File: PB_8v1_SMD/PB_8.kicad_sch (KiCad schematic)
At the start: 26 parts, among them J18 Power In Right, J23 VIN Voltage, J25 RTC Conn, J26 OLED Conn, J27 GPIO Header, J28 Aux Pwr, J29 VIN Select, Q1 DMP3056L, SW1 Enter BTN, SW2 Down BTN, SW3 OLED Select, U1 OKI-78SR-5, U2 24LC256

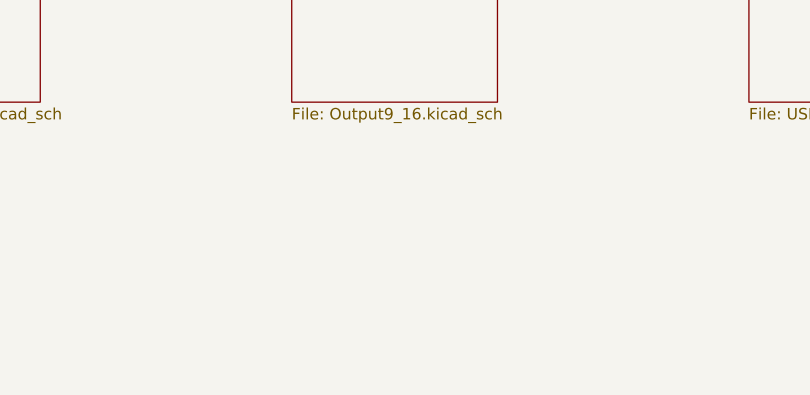
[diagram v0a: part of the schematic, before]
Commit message: Add Diff out 9-12
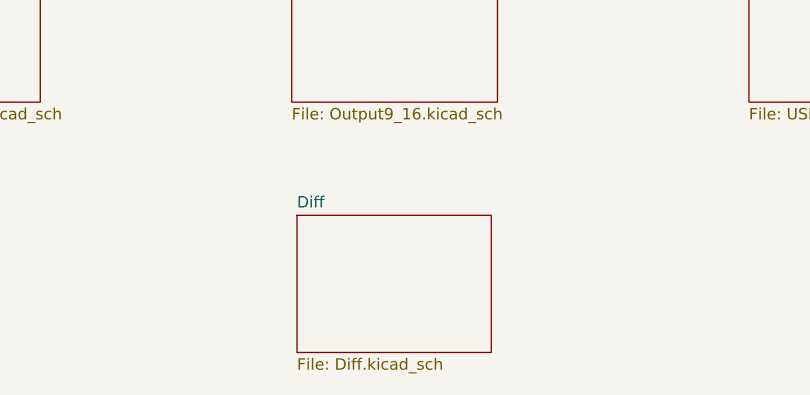
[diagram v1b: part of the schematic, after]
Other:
- added sheet Diff (Diff.kicad_sch)
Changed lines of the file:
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@@
+    )
+  )
+  (sheet (at 87.3252 177.292) (size 21.59 15.24) (fields_autoplaced)
+    (stroke (width 0) (type solid) (color 0 0 0 0))
+    (fill (color 0 0 0 0.0000))
+    (property "Sheet name" "Diff" (id 0) (at 87.3252 176.5804 0)
+      (effects (font (size 1.27 1.27)) (justify left bottom))
+    )
+    (property "Sheet file" "Diff.kicad_sch" (id 1) (at 87.3252 193.1166 0)
+      (effects (font (size 1.27 1.27)) (justify left top))
     )
   )
@@
     (path "/" (page "1"))
     (path "/00000000-0000-0000-0000-00005d413c25" (page "2"))
+    (path "/ee281e36-0822-48a2-9e3f-ba9140af478c" (page "3"))
     (path "/00000000-0000-0000-0000-00005d4698de" (page "4"))
     (path "/00000000-0000-0000-0000-00005d648680" (page "6"))
   )
   (symbol_instances
+    (path "/ee281e36-0822-48a2-9e3f-ba9140af478c/97fca2e9-9c9d-485a-af6f-c9d488a151a9"
+      (reference "#PWR01") (unit 1) (value "+5V") (footprint "")
+    )
     (path "/00000000-0000-0000-0000-00005d5b866e"
       (reference "#PWR02") (unit 1) (value "GND") (footprint "")
     )
+    (path "/ee281e36-0822-48a2-9e3f-ba9140af478c/39d41e00-f438-4796-a9cd-e6f3168c73de"
+      (reference "#PWR03") (unit 1) (value "GND") (footprint "")
+    )
     (path "/00000000-0000-0000-0000-00005d51c5e3"
       (reference "#PWR04") (unit 1) (value "GND") (footprint "")
@@
       (reference "#PWR032") (unit 1) (value "+3.3V") (footprint "")
     )
+    (path "/ee281e36-0822-48a2-9e3f-ba9140af478c/78855180-3489-4b90-8473-a0526a6cdc7e"
+      (reference "#PWR033") (unit 1) (value "+5V") (footprint "")
+    )
+    (path "/ee281e36-0822-48a2-9e3f-ba9140af478c/8ec2d9bf-7f3e-41fd-b41a-95a7b12782d3"
+      (reference "#PWR034") (unit 1) (value "GND") (footprint "")
+    )
     (path "/00000000-0000-0000-0000-00005d413c25/00000000-0000-0000-0000-00005e95876a"
       (reference "#PWR038") (unit 1) (value "GND") (footprint "")
@@
       (reference "C4") (unit 1) (value "0.1uF") (footprint "Capacitor_SMD:C_0603_1608Metric_Pad1.08x0.95mm_HandSolder")
     )
+    (path "/ee281e36-0822-48a2-9e3f-ba9140af478c/9afffebf-f2b4-422d-b595-02654a91f956"
+      (reference "C5") (unit 1) (value "0.1uF") (footprint "Capacitor_SMD:C_0603_1608Metric_Pad1.08x0.95mm_HandSolder")
+    )
     (path "/00000000-0000-0000-0000-00005d4698de/00000000-0000-0000-0000-00005d4e3ada"
       (reference "C6") (unit 1) (value "0.1uF") (footprint "Capacitor_SMD:C_0603_1608Metric_Pad1.08x0.95mm_HandSolder")
@@
       (reference "J8") (unit 1) (value "String8") (footprint "Connector_Phoenix_MC:PhoenixContact_MCV_1,5_3-G-3.5_1x03_P3.50mm_Vertical")
     )
+    (path "/ee281e36-0822-48a2-9e3f-ba9140af478c/383a15f1-ee32-4530-bca5-9032d1bb1254"
+      (reference "J9") (unit 1) (value "RJ45") (footprint "Connector_RJ:RJ45_Amphenol_54602-x08_Horizontal")
+    )
     (path "/00000000-0000-0000-0000-00005ecf4c8a"
       (reference "J18") (unit 1) (value "Power In Right") (footprint "Barrier_Blocks:BARRIER_BLOCK_1ROW_2POS_P9.5MM")
@@
       (reference "R1") (unit 1) (value "1K") (footprint "Resistor_SMD:R_0603_1608Metric_Pad0.98x0.95mm_HandSolder")
     )
+    (path "/ee281e36-0822-48a2-9e3f-ba9140af478c/95903096-7705-43fe-ba46-051e52f59cc0"
+      (reference "R2") (unit 1) (value "120") (footprint "Resistor_SMD:R_0603_1608Metric_Pad0.98x0.95mm_HandSolder")
+    )
     (path "/00000000-0000-0000-0000-00005d66016d"
       (reference "R3") (unit 1) (value "120") (footprint "Resistor_SMD:R_0603_1608Metric_Pad0.98x0.95mm_HandSolder")
@@
       (reference "R6") (unit 1) (value "4.7K") (footprint "Resistor_SMD:R_0603_1608Metric_Pad0.98x0.95mm_HandSolder")
     )
+    (path "/ee281e36-0822-48a2-9e3f-ba9140af478c/702edc17-db40-4cca-a32a-30256961ef23"
+      (reference "R7") (unit 1) (value "120") (footprint "Resistor_SMD:R_0603_1608Metric_Pad0.98x0.95mm_HandSolder")
+    )
+    (path "/ee281e36-0822-48a2-9e3f-ba9140af478c/a8720fe1-0906-45d8-bbfe-4e8d6b04c8fd"
+      (reference "R8") (unit 1) (value "120") (footprint "Resistor_SMD:R_0603_1608Metric_Pad0.98x0.95mm_HandSolder")
+    )
+    (path "/ee281e36-0822-48a2-9e3f-ba9140af478c/898b0d0d-cb93-4f5a-8a16-1f96efe50bf5"
+      (reference "R9") (unit 1) (value "120") (footprint "Resistor_SMD:R_0603_1608Metric_Pad0.98x0.95mm_HandSolder")
+    )
     (path "/00000000-0000-0000-0000-00005d4698de/550703a5-aa76-411e-90fc-4363b6cc0176"
       (reference "R15") (unit 1) (value "33") (footprint "Resistor_SMD:R_0603_1608Metric_Pad0.98x0.95mm_HandSolder")
@@
       (reference "U3") (unit 2) (value "POCKETBEAGLE-SC-569") (footprint "POCKETBEAGLE:BEAGLE_POCKETBEAGLE-SC-569")
     )
+    (path "/ee281e36-0822-48a2-9e3f-ba9140af478c/74ae4135-4e09-4370-9ec7-99e88e06c12a"
+      (reference "U4") (unit 1) (value "AM26C31") (footprint "Package_SO:SOIC-16_3.9x9.9mm_P1.27mm")
+    )
     (path "/00000000-0000-0000-0000-00005d4698de/00000000-0000-0000-0000-00005d4e3af4"
